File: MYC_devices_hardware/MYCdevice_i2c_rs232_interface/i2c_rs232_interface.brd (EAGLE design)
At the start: 90.8 x 53 mm, 60 parts, among them IC1 MEGA32-P, IC2 MAX232, IC3 7805TV, Q1 20MHz, T1 BC817, T2 BC817, T3 BC817, T4 BC807, T5 BC817-40LT1SMD, T6 BC817-40LT1SMD, X1 8-15V, X2 1503_09, X3 1503_09, X4 RS232

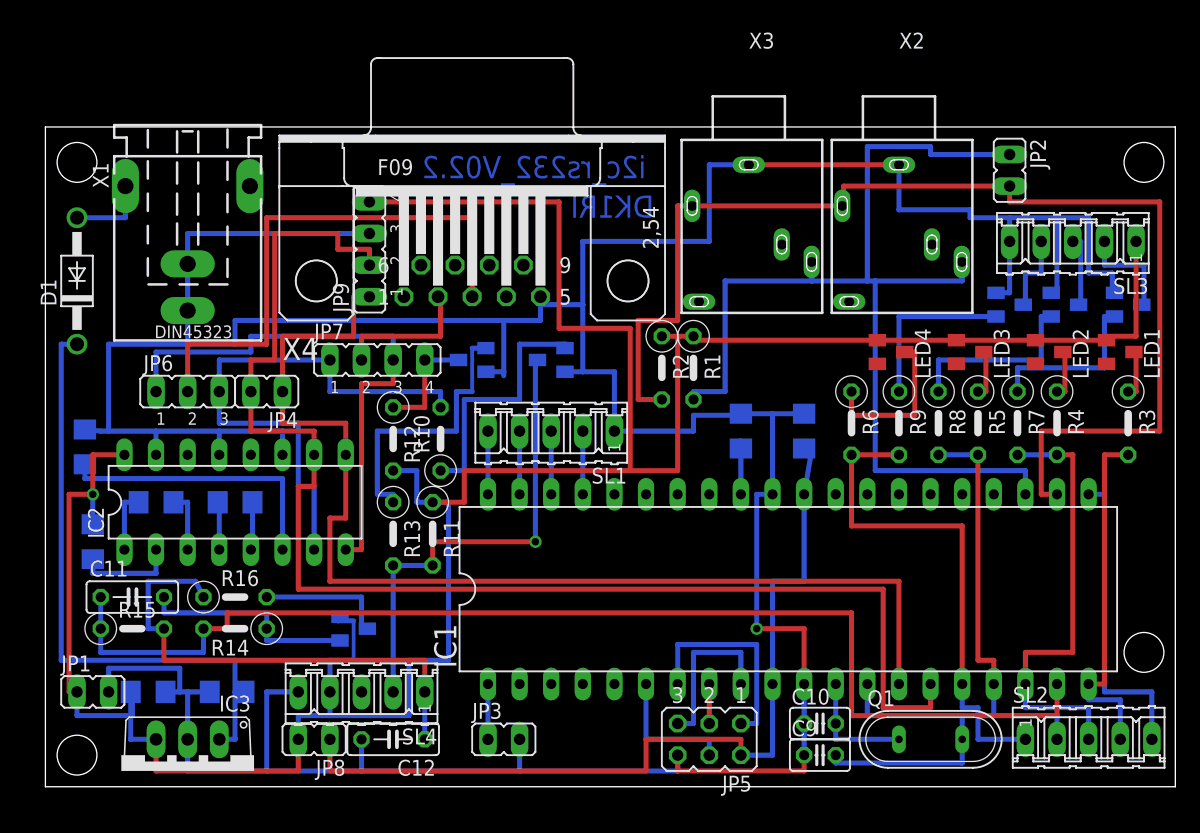
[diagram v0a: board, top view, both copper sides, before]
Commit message: HW changed and 254 /255 command croorected
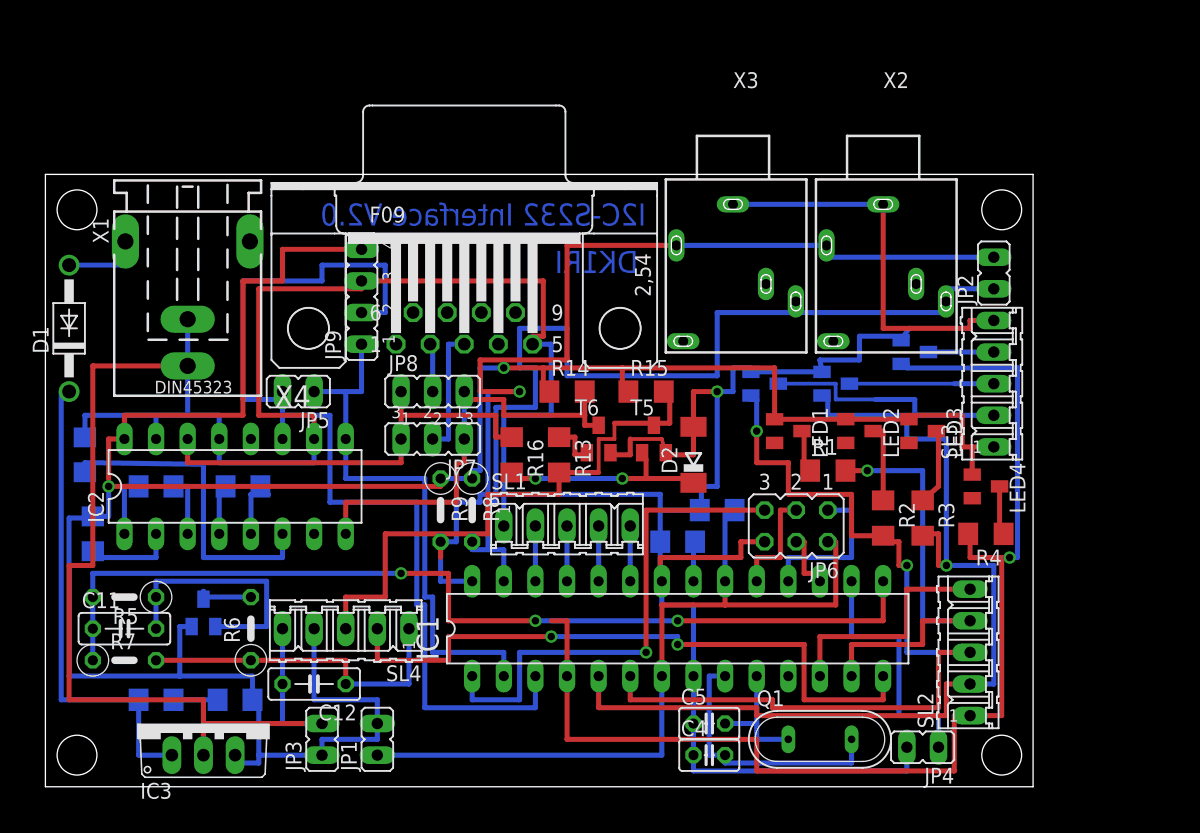
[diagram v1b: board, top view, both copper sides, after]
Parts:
- removed R10, R11, R12: 4k7, resistor:0207/5V
- added D2: (no value), diode:SOD106-R
- C1, C2: value 22uF -> 22uF 1210
- C10, C9: value 18pF -> 22u 1210; device resistor:C025-025X050 -> rcl:C1206
- C3, C6: value 22u -> 22uF 1210
- C4, C5: value 22u -> 18pF; device rcl:C1206 -> resistor:C025-025X050
- C7, C8: value 22uF -> 22u 1210
- IC1: value MEGA32-P -> MEGA8-P; device atmel:DIL40 -> atmel:DIL28-3
- JP1: value 5V -> Power
- JP3: value Reset -> 5V
- JP4: value I2C -> Reset
- JP5: value ISP -> Rs232-TTL; device jumper:JP3Q -> jumper:JP1
- JP6: value DTE/DCE -> ISP; device jumper:JP2 -> jumper:JP3Q
- JP7: device jumper:JP4 -> jumper:JP2
- JP8: value Power -> DTE/DCE; device jumper:JP1 -> jumper:JP2
- JP9: value RS232-USB -> USB
- R1, R13, R2, R3, R4: device resistor:0207/5V -> resistor:R1206
- R14, R15: value 10k -> 4k7; device resistor:0207/5V -> resistor:R1206
- R16: value 10 -> 10k; device resistor:0207/5V -> resistor:R1206
- R5, R7: value 4k7 -> 10k
- R6: value 4k7 -> 10
- T1, T2, T3: value BC817 -> BC817 SOT23
- T4: value BC807 -> BC807 SOT23
- T5, T6: value BC817-40LT1SMD -> BC817 SOT23; device transistor-npn:SOT23-BEC -> transistor:SOT23-BEC
- moved R7 74.2 mm to (6.35, 10.2), turned to 0 degrees
- moved R5 70.0 mm to (6.35, 15.2), turned to 180 degrees
- moved C10 62.9 mm to (3.17, 26.7), flipped to the bottom, turned to 270 degrees
- moved C9 61.1 mm to (3.81, 20.3), flipped to the bottom, turned to 90 degrees
- moved JP4 60.0 mm to (70.5, 3.17)
- moved C7 52.3 mm to (8.89, 24.1), turned to 180 degrees
- moved C5 51.6 mm to (53.3, 5.08), flipped to the top, turned to 0 degrees
- moved C6 51.1 mm to (54.0, 22.2), turned to 0 degrees
- moved R6 51.0 mm to (16.5, 12.7), turned to 90 degrees
- moved JP6 50.1 mm to (60.3, 21.0), turned to 180 degrees
- moved R15 45.5 mm to (48.3, 31.8)
- moved JP5 43.3 mm to (20.3, 31.8), turned to 90 degrees
- moved C4 43.2 mm to (53.3, 2.54), flipped to the top, turned to 0 degrees
- moved C3 42.0 mm to (50.8, 19.7)
- moved C8 40.3 mm to (15.9, 24.1), turned to 180 degrees
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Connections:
- removed net N$11: IC2.8, JP6.1, JP7.3
- removed net N$21: JP7.4, R12.1, T6.C
- removed net N$24: R7.1, T1.B
- removed net N$27 (its old number): IC1.14, IC2.9, JP4.1, JP9.1
- removed net N$36: R11.2, R13.2, SL4.2, T5.C
- removed net N$40: R9.1, T3.B
- removed net N$42 (its old number): C8.2, IC1.32
- removed net N$55: C10.2, IC1.12, Q1.1
- removed net N$58: C7.1, IC1.10, IC1.30, JP5.2, JP8.1
- new net N$10: IC2.14, JP7.3, JP8.1, R16.1
- new net N$37: C5.2, IC1.10, Q1.1
- new net N$38: D2.C, R16.2, T5.B
- new net N$44: C6.1, IC1.20, IC1.7, JP1.1, JP6.2
- new net N$53: R13.2, R15.2, SL4.3, T5.C
- new net N$7: IC1.14, SL4.2
- net C13: now also C7.1; no longer C3.1
- net GND: now also C3.1, C4.1, C5.1, C6.2, D2.A, IC1.22, IC1.8, IC2.10, JP4.2, JP6.6; no longer C6.1, C7.2, C8.1, C9.1, IC1.11, IC1.31, IC2.11, JP1.2, JP5.6
- net N$1: now also IC1.13, R1.2; no longer IC1.20, R3.2
- net N$12: now also IC1.3, IC2.11, JP5.2, JP9.2; no longer R8.1, T2.B
- net N$13: now also C8.1; no longer C4.1
- net N$14: now also C7.2; no longer C3.2
- net N$15: now also IC1.18, JP6.1; no longer IC1.7, JP5.1
- net N$16: now also C9.1; no longer C5.1
- net N$17: now also C10.2; no longer C6.2
- net N$18: now also IC1.1, JP6.5; no longer IC1.9, JP5.5
- net N$19: now also C4.2, IC1.9; no longer C9.2, IC1.13
- net N$2: now also IC1.2, IC2.9, JP5.1, JP9.1; no longer IC2.7, JP6.3, JP7.1, R10.2
- net N$20: now also IC1.19, JP6.3; no longer IC1.8, JP5.3
- net N$22: now also IC1.28, R9.2; no longer IC1.22, R2.2
- net N$23: now also IC1.6, R2.2, T1.B; no longer IC1.18, R4.2, R7.2
- net N$25: now also IC1.24; no longer IC1.39
- net N$26: now also IC1.25; no longer IC1.38
- net N$28: now also IC1.17, JP6.4; no longer IC1.6, JP5.4
- net N$29: now also R5.1; no longer R14.1
- net N$3: now also C8.2; no longer C4.2
- net N$30: now also IC1.15, R5.2, R7.1; no longer IC1.19, R14.2, R15.1
- net N$31: now also R6.2; no longer R16.2
- net N$32: now also R6.1, R7.2; no longer R15.2, R16.1
- net N$34: now also IC1.23; no longer IC1.40
- net N$35: now also C3.2, IC1.21; no longer IC1.15, IC2.10, JP4.2, JP9.2
- net N$39: now also IC1.26; no longer IC1.37
- net N$4: now also JP8.2; no longer JP7.2
- net N$41: now also IC2.8, JP7.1, JP8.3, R14.2, T6.C; no longer R10.1, T5.B
- net N$43: now also R4.1; no longer R6.1
- net N$48: now also R3.1; no longer R5.1
- net N$49: now also R2.1; no longer R4.1
- net N$5: now also IC1.27, R8.2; no longer IC1.23, R1.2
- net N$50: now also R1.1; no longer R3.1
- net N$51: now also IC1.5, R3.2, T2.B; no longer IC1.17, R5.2, R8.2
- net N$52: now also IC1.4, R4.2, T3.B; no longer IC1.16, R6.2, R9.2
- net N$6: now also IC1.16, JP4.1; no longer IC1.1, JP3.1
- net N$8: now also IC1.12; no longer IC1.21
- net N$9: now also JP7.2; no longer JP6.2
- net VDD: now also C9.2, JP1.2, JP3.1, R14.1, R15.1, R8.1, R9.1; no longer C5.2, JP1.1, JP8.2, R1.1, R11.1, R12.2, R2.1
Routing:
- net N$35: track 109.2 -> 3.30 mm
- net N$27 (its old number): track 90.2 -> 0.00 mm
- net N$58: track 69.8 -> 0.00 mm
- net N$12: track 15.1 -> 81.9 mm
- net N$44: track 0.00 -> 63.0 mm
- net N$52: track 40.6 -> 96.2 mm, vias 0 -> 1
- net N$7: track 0.00 -> 52.1 mm, vias 0 -> 2
- net N$51: track 32.4 -> 79.0 mm, vias 0 -> 1
- net N$53: track 0.00 -> 45.7 mm
- net N$11: track 44.5 -> 0.00 mm
- net N$36: track 38.3 -> 0.00 mm, vias 1 -> 0
- net N$23: track 36.2 -> 72.5 mm, vias 0 -> 2
- net N$10: track 0.00 -> 35.4 mm
- net N$9: track 43.2 -> 10.2 mm
- net N$18: track 13.3 -> 40.6 mm, vias 0 -> 1
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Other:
- board size 90.8 x 53 mm -> 79.4 x 49.2 mm
- board text added: "I2C-S232 Interface V2.0"
- board text removed: "i2c_rs232_V02.2"

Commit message: Electronic load added; error correction and minor enhancements for I2C Interface
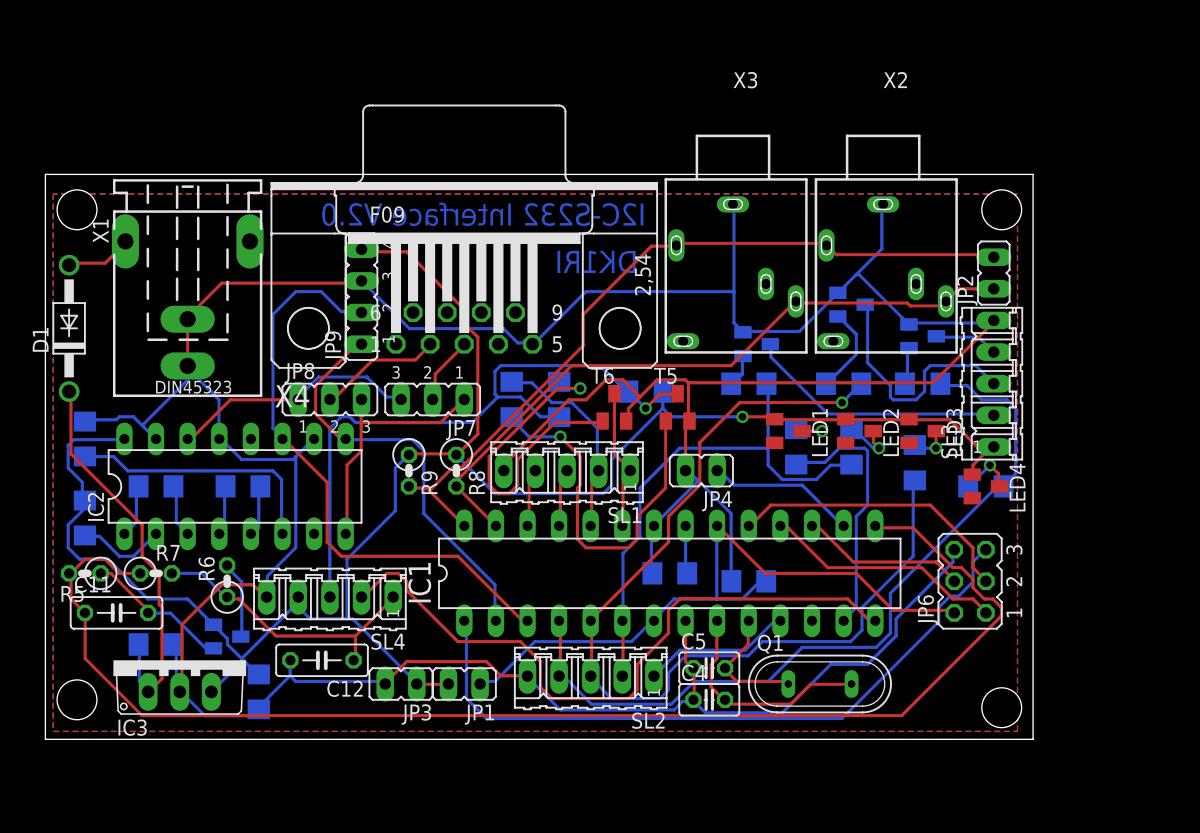
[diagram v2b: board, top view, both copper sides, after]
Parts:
- removed D2: (no value), diode:SOD106-R
- removed JP5: Rs232-TTL, jumper:JP1
- removed R14: 4k7, resistor:R1206
- added R10, R11, R12: 4k7, resistor:R1206
- R13: value 4k7 -> 10k
- R5, R6, R7, R8, R9: device resistor:0207/5V -> resistor:0207/2V
- SL1: value GPIO -> GPIO1
- SL2: value Mast -> GPIO2
- moved SL2 30.5 mm to (43.8, 8.89), turned to 180 degrees
- moved JP4 28.5 mm to (52.7, 25.4)
- moved JP6 14.7 mm to (74.3, 16.5), turned to 90 degrees
- moved JP1 8.28 mm to (33.7, 8.26), turned to 90 degrees
- moved JP8 8.28 mm to (22.9, 31.1)
- moved JP3 7.75 mm to (28.6, 8.26), turned to 90 degrees
- moved R7 7.43 mm to (8.89, 17.1)
- moved T2 6.48 mm to (64.8, 38.7)
- moved R2 6.25 mm to (64.8, 27.3), flipped to the bottom
- moved C6 6.25 mm to (56.5, 16.5)
- moved IC3 5.43 mm to (10.8, 10.2)
- moved R3 4.49 mm to (69.8, 26.0), flipped to the bottom
- moved IC1 4.49 mm to (50.2, 17.1)
- moved C4 4.45 mm to (53.3, 6.99)
- moved C5 4.45 mm to (53.3, 9.53)
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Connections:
- new net N$11: IC1.23, SL1.1, T6.C
- new net N$21: IC1.11, SL2.1
- new net N$24: R12.1, T3.B
- net GND: now also SL1.5, SL2.5; no longer D2.A, SL1.1
- net N$1: no longer SL2.4
- net N$10: no longer R16.1
- net N$12: no longer JP5.2
- net N$2: no longer JP5.1
- net N$23: now also R10.2, SL2.2; no longer SL2.3, T1.B
- net N$25: now also R16.1, SL1.2; no longer SL1.4
- net N$34: now also R11.1, T2.B; no longer IC1.23, SL1.5
- net N$38: no longer D2.C
- net N$39: now also SL1.4; no longer SL1.2
- net N$41: no longer R14.2, T6.C
- net N$51: now also R11.2, SL2.3; no longer SL2.2, T2.B
- net N$52: now also R12.2, SL2.4; no longer SL2.1, T3.B
- net N$8: now also R10.1, T1.B; no longer IC1.12, SL2.5
- net VDD: no longer R14.1
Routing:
- net VDD: track 206.8 -> 157.3 mm, vias 2 -> 1
- net N$12: track 81.9 -> 47.4 mm
- net GND: track 345.3 -> 311.8 mm, vias 1 -> 0
- net N$52: track 96.2 -> 63.9 mm, vias 1 -> 0
- net N$23: track 72.5 -> 41.6 mm, vias 2 -> 0
- net N$30: track 77.5 -> 106.8 mm, vias 3 -> 0
- net N$5: track 78.4 -> 54.8 mm
- net N$42: track 4.61 -> 26.8 mm, vias 0 -> 1
- net N$22: track 82.5 -> 61.4 mm, vias 1 -> 0
- net N$8: track 19.1 -> 2.68 mm
- net N$41: track 36.4 -> 20.4 mm
- net N$18: track 40.6 -> 56.0 mm, vias 1 -> 0
- net N$1: track 36.0 -> 20.9 mm, vias 1 -> 0
- net N$10: track 35.4 -> 20.3 mm
- net N$20: track 8.89 -> 23.2 mm
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- added copper zone on layer 1, net GND
- added copper zone on layer 16, net GND
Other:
- board size 79.4 x 49.2 mm -> 79.4 x 45.4 mm

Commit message: new connectors, I2c with 3V
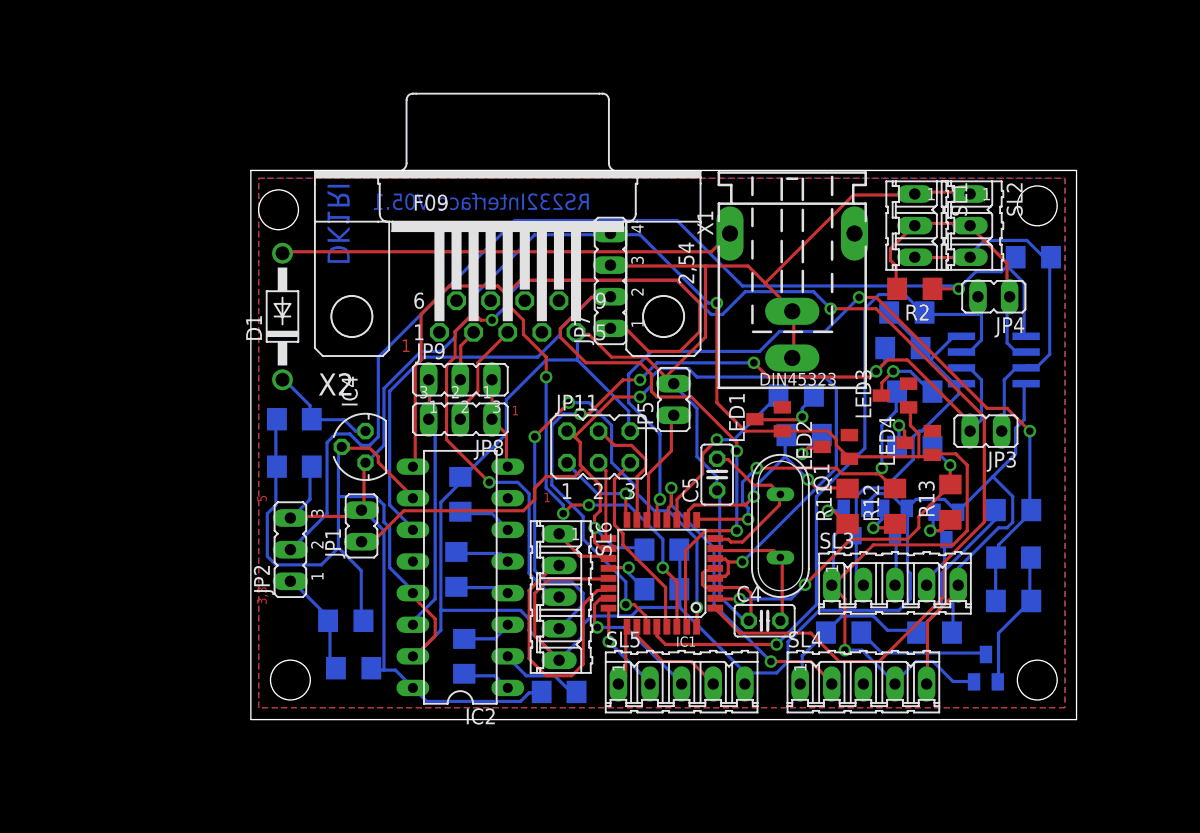
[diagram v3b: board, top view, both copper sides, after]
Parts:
- removed JP6: ISP, jumper:JP3Q
- removed T5, T6: BC817 SOT23, transistor:SOT23-BEC
- removed X3: 1503_09, con-lumberg:1503_09
- removed X4: RS232, con-subd:F09H
- added IC4: 78L05, v-reg:78LXX
- added JP11: (no value), jumper:JP3Q
- added JP5: Reset, jumper:JP1
- added R14: 10k, resistor:R1206
- added SL5: GPIO1, con-amp-quick:05P
- added SL6: GPIO2, con-amp-quick:05P
- C1, C2, C6: value 22uF 1210 -> 22u
- C10: value 22u 1210 -> 22uF
- C11, C12: device resistor:C050-025X075 -> resistor:C1206
- C7, C8, C9: value 22u 1210 -> 22u
- IC1: value MEGA8-P -> MEGA8-AI; device atmel:DIL28-3 -> atmel:TQFP32-08
- IC3: value 7805TV -> PCA9517; device linear:TO220V -> PCA9517:SO-08
- JP2: value I2C -> 3V/5V; device jumper:JP1 -> jumper:JP2
- JP3: value 5V -> SDA
- JP4: value Reset -> SCL
- JP7: value DTE/DCE -> USB; device jumper:JP2 -> jumper:JP4
- JP9: value USB -> DTE/DCE; device jumper:JP4 -> jumper:JP2
- R1, R2, R3, R4: value 4k7 -> see manual
- R13: value 10k -> 4k7
- R15: value 4k7 -> 10k
- R16: value 10k -> 10
- R5: value 10k -> 1k; device resistor:0207/2V -> resistor:R1206
- R6: value 10 -> 1k5; device resistor:0207/2V -> resistor:R1206
- R7: value 10k -> 4k7; device resistor:0207/2V -> resistor:R1206
- R8, R9: device resistor:0207/2V -> resistor:R1206
- SL1: value GPIO1 -> I2C1; device con-amp-quick:05P -> con-amp-quick:03P
- SL2: value GPIO2 -> I2C2; device con-amp-quick:05P -> con-amp-quick:03P
- X2: value 1503_09 -> RS232; device con-lumberg:1503_09 -> con-subd:F09H
- moved C11 72.2 mm to (77.8, 18.4), flipped to the bottom, turned to 180 degrees
- moved IC3 69.7 mm to (76.2, 34.3), flipped to the bottom, turned to 270 degrees
- moved T4 61.0 mm to (75.6, 9.53), turned to 0 degrees
- moved JP2 60.7 mm to (19.7, 19.1), turned to 90 degrees
- moved R7 53.4 mm to (60.3, 31.4), flipped to the bottom
- moved JP3 51.2 mm to (75.6, 28.6)
- moved C12 49.3 mm to (71.4, 12.4), flipped to the bottom
- moved X1 48.6 mm to (60.0, 44.5)
- moved SL2 47.3 mm to (74.3, 45.1), turned to 270 degrees
- moved C10 47.2 mm to (49.5, 19.1), turned to 180 degrees
- moved SL4 43.4 mm to (65.7, 8.26), turned to 0 degrees
- moved R9 41.1 mm to (69.8, 31.8), flipped to the bottom, turned to 0 degrees
- moved SL1 34.2 mm to (69.8, 45.1), turned to 270 degrees
- moved R16 32.6 mm to (64.1, 12.4), turned to 180 degrees
- moved R13 32.5 mm to (72.7, 22.9), flipped to the top, turned to 90 degrees
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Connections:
- new net N$36: IC1.24, SL5.2
- new net N$40: IC1.1, SL6.3
- new net N$54: IC1.22, SL6.2
- new net N$56: IC3.1, JP2.2, R1.1, R2.1
- net C13: now also C6.1; no longer C7.1
- net GND: now also C10.2, C9.1, IC1.21, IC1.3, IC1.5, IC3.4, IC4.GND, JP11.6, JP5.2, JP7.3, R6.2, SL1.1, SL2.1, SL5.5, SL6.5, X2.5; no longer C10.1, C6.2, IC1.22, IC1.8, IC3.2, JP3.2, JP4.2, JP6.6, JP9.3, SL1.5, SL2.5, T5.E, T6.E, X2.1, X3.1, X4.5
- net N$1: now also IC1.11, R7.2; no longer IC1.13, R1.2
- net N$10: now also JP8.3, JP9.1; no longer JP7.3, JP8.1
- net N$11: now also C10.1, IC1.18, IC1.4, IC1.6, JP1.1, JP11.2; no longer IC1.23, SL1.1, T6.C
- net N$12: now also IC1.31, JP7.2; no longer IC1.3, JP9.2
- net N$13: now also C7.1; no longer C8.1
- net N$14: now also C6.2; no longer C7.2
- net N$15: now also IC1.16, JP11.1; no longer IC1.18, JP6.1
- net N$16: now also C8.1; no longer C9.1
- net N$17: now also C9.2; no longer C10.2
- net N$18: now also IC1.29, JP11.5; no longer IC1.1, JP6.5
- net N$19: now also IC1.7; no longer IC1.9
- net N$2: now also IC1.30, JP7.1; no longer IC1.2, JP9.1
- net N$20: now also IC1.17, JP11.3; no longer IC1.19, JP6.3
- net N$21: now also IC1.19, SL6.1; no longer IC1.11, SL2.1
- net N$22: now also IC3.7, JP4.2, R3.2; no longer JP2.2, R9.2, X2.2, X3.2
- net N$23: now also IC1.10, R11.2, R8.2; no longer IC1.6, R10.2, R2.2, SL2.2
- net N$24: now also R13.1; no longer R12.1
- net N$25: now also IC1.9, R12.2, R9.2; no longer IC1.24, R16.1, SL1.2
- net N$26: now also IC1.23, SL5.3; no longer IC1.25, SL1.3
- net N$28: now also IC1.15, JP11.4; no longer IC1.17, JP6.4
- net N$29: now also R14.1; no longer R5.1
- net N$3: now also C7.2; no longer C8.2
- net N$30: now also IC1.13, R14.2, R15.1; no longer IC1.15, R5.2, R7.1
- net N$31: now also R16.2; no longer R6.2
- net N$32: now also R15.2, R16.1; no longer R6.1, R7.2
- net N$33: now also IC4.IN; no longer IC3.1
- net N$34: now also R12.1; no longer R11.1
- net N$35: now also IC1.20; no longer IC1.21
- net N$37: now also IC1.8; no longer IC1.10
- net N$38: now also IC3.2, JP4.1, R2.2, SL1.2, SL2.2; no longer R16.2, T5.B
- net N$39: now also SL5.4; no longer SL1.4
- net N$4: now also JP9.2, X2.2; no longer JP8.2, X4.2
- net N$41: now also JP8.1, JP9.3; no longer JP7.1, JP8.3
- net N$42: now also IC1.12, SL4.2; no longer R13.1, T6.B
- net N$43: now also R10.1; no longer R4.1
- net N$44: now also IC3.3, JP3.1, R1.2, SL1.3, SL2.3; no longer C6.1, IC1.20, IC1.7, JP1.1, JP6.2
- net N$48: now also R9.1; no longer R3.1
- net N$49: now also R8.1; no longer R2.1
- net N$5: now also IC3.6, JP3.2, R4.2; no longer JP2.1, R8.2, X2.3, X3.3
- net N$50: now also R7.1; no longer R1.1
- net N$51: now also IC1.32, SL6.4; no longer IC1.5, R11.2, R3.2, SL2.3
- net N$52: now also IC1.2, R10.2, R13.2; no longer IC1.4, R12.2, R4.2, SL2.4
- net N$53: now also JP2.1, R5.2, R6.1; no longer R13.2, R15.2, SL4.3, T5.C
- net N$6: now also IC1.14, JP5.1; no longer IC1.16, JP4.1
- net N$7: now also IC1.25, SL5.1; no longer IC1.14, SL4.2
- net N$8: now also R11.1; no longer R10.1
- net N$9: now also JP8.2, X2.3; no longer JP7.2, X4.3
- net VDD: now also C8.2, IC3.5, IC3.8, IC4.OUT, JP2.3, JP7.4, R3.1, R4.1, R5.1; no longer C9.2, IC3.3, JP3.1, JP9.4, R15.1, R8.1, R9.1
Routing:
- net N$40: track 0.00 -> 116.0 mm, vias 0 -> 3
- net N$56: track 0.00 -> 89.9 mm, vias 0 -> 1
- net N$11: track 11.4 -> 83.0 mm, vias 0 -> 3
- net N$2: track 33.4 -> 84.7 mm, vias 0 -> 4
- net N$7: track 54.1 -> 4.89 mm
- net N$53: track 53.0 -> 8.72 mm, vias 1 -> 0
- net N$18: track 56.0 -> 15.4 mm
- net N$30: track 106.8 -> 67.1 mm, vias 0 -> 3
- net N$52: track 63.9 -> 26.9 mm, vias 0 -> 3
- net VDD: track 157.3 -> 190.9 mm, vias 1 -> 2
- net N$27: track 5.38 -> 36.6 mm
- net N$51: track 76.9 -> 46.8 mm, vias 1 -> 3
- net N$12: track 47.4 -> 75.3 mm, vias 0 -> 2
- net N$44: track 54.4 -> 29.0 mm
- net N$23: track 41.6 -> 18.6 mm, vias 0 -> 2
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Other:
- board size 79.4 x 45.4 mm -> 66.3 x 44.1 mm
- board text added: "1"
- board text added: "3,3"
- board text added: "5"
- board text added: "RS232Interface V05.1"
- board text removed: "I2C-S232 Interface V2.0"
